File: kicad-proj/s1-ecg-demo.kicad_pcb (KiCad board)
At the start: 4 copper layers, 80.2 x 30.2 mm, 54 parts, among them J1 USB-C-16-Pin, J2 TC2030, J3 Battery Port, J4 Current Probe, J5 ECG_PAD_LA, J6 ECG_PAD_RA, J7 ECG_PAD_RL, U1 AD8233

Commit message: Layout complete, needs checking
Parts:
- removed the R14 at (116.3, 60.6)
- removed the R15 at (114.9, 61.4)
- removed the R16 at (114.9, 59.5)
- removed the R23 at (116.4, 65.0)
- removed the R4 at (118.0, 61.6)
- removed the R6 at (117.7, 64.5)
- removed the TP5 at (113.7, 68.7)
- added FID1: Logo, s1-ecg-demo:sw-logo, B.Cu at (110.9, 103.2)
- added FID2: Board title, s1-ecg-demo:title, B.Cu at (117.2, 103.8)
- added FID3: Heartbeat icon, s1-ecg-demo:heartbeat, F.Cu at (134.8, 106.8)
- added R18: 10M, Resistor_SMD:R_0201_0603Metric, F.Cu at (147.8, 102.7)
- added R19: 10M, Resistor_SMD:R_0201_0603Metric, F.Cu at (146.4, 103.5)
- added R2: 200k, Resistor_SMD:R_0201_0603Metric, F.Cu at (147.8, 101.8)
- added R21: 10M, Resistor_SMD:R_0201_0603Metric, F.Cu at (146.4, 101.6)
- added R22: 5.1k, Resistor_SMD:R_0201_0603Metric, F.Cu at (135.7, 110.3)
- added R3: 499k, Resistor_SMD:R_0201_0603Metric, F.Cu at (150.4, 108.2)
- added TP2: D1, TestPoint:TestPoint_Pad_D1.0mm, B.Cu at (127.4, 106.5)
- J1: renamed from J5; value ECG_PAD_LA -> Left arm
- J2: renamed from J6; value ECG_PAD_RA -> Right arm
- J3: renamed from J7; value ECG_PAD_RL -> Right leg
- JP1: moved to B.Cu
- R1: value 5.1k -> 100k
- R10: value 499k -> 1M
- R11: value 1M -> 182k
- R13: value 182k -> 100k
- R5: value 200k -> 10M
- R7: value 10M -> 100k
- R8: value 100k -> 1M
- R9: value 1M -> 10M
- TP1: value Tp -> ECG out; footprint TestPoint:TestPoint_Pad_1.0x1.0mm -> TestPoint:TestPoint_Pad_D1.0mm; moved to B.Cu
- TP3: renamed from TP2; value Tp -> D2; footprint TestPoint:TestPoint_Pad_1.0x1.0mm -> TestPoint:TestPoint_Pad_D1.0mm; moved to B.Cu
- TP4: renamed from TP3; value Tp -> D3; footprint TestPoint:TestPoint_Pad_1.0x1.0mm -> TestPoint:TestPoint_Pad_D1.0mm; moved to B.Cu
- TP5: renamed from TP4; value Tp -> D4; footprint TestPoint:TestPoint_Pad_1.0x1.0mm -> TestPoint:TestPoint_Pad_D1.0mm; moved to B.Cu
- moved FID4 93.5 mm to (158.2, 117.9)
- moved TP1 75.1 mm to (152.1, 112.8), turned to 0 degrees
- moved TP5 63.1 mm to (127.4, 112.8), turned to 90 degrees
- moved TP4 58.4 mm to (127.4, 110.7), turned to 90 degrees
- moved TP3 58.4 mm to (127.4, 108.6), turned to 90 degrees
- moved R5 57.3 mm to (149.2, 106.6)
- moved FID5 54.9 mm to (120.1, 89.3)
- moved R9 54.4 mm to (150.4, 105.3), turned to 270 degrees
- moved R12 53.3 mm to (149.2, 105.7)
- moved R13 53.0 mm to (147.9, 107.1), turned to 90 degrees
- moved R1 52.7 mm to (149.6, 103.7), turned to 180 degrees
- moved C5 52.6 mm to (147.8, 103.7)
- moved C7 52.6 mm to (145.4, 101.4)
- moved C2 52.6 mm to (145.6, 107.6)
- moved C3 52.6 mm to (149.4, 108.0)
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- renumbered FID3 to FID4, FID4 to FID5, J1 to J4, J2 to J5, J4 to J6, J3 to J7, D1 to LED1, D2 to LED2, D3 to LED3, D4 to LED4, D5 to LED5, D6 to LED6, D7 to LED7, R18 to R14, R19 to R15, R20 to R16, R21 to R17, R22 to R20, R2 to R23, R3 to R4, R17 to R6
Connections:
- net /SWDCLK renamed Net-(J5-Pad4)
- net /SWDIO renamed Net-(J5-Pad2)
- J1 pad 1: Net-(J5-Pad1) -> Net-(J1-Pad1)
- J2 pad 1: Net-(J6-Pad1) -> Net-(J2-Pad1)
- J3 pad 1: Net-(J7-Pad1) -> Net-(J3-Pad1)
- J4 pad A5: Net-(J1-PadA5) -> Net-(J4-PadA5)
- R1 pad 1: GND -> Net-(C1-Pad1)
- R1 pad 2: Net-(J1-PadA5) -> Net-(C4-Pad1)
- R10 pad 1: Net-(C3-Pad1) -> Net-(C4-Pad2)
- R10 pad 2: Net-(J7-Pad1) -> Net-(C2-Pad2)
- R11 pad 1: Net-(C4-Pad2) -> Net-(R11-Pad1)
- R11 pad 2: Net-(C2-Pad2) -> Net-(J1-Pad1)
- R12 pad 2: Net-(J5-Pad1) -> Net-(J2-Pad1)
- R13 pad 1: Net-(R13-Pad1) -> Net-(C4-Pad1)
- R13 pad 2: Net-(J6-Pad1) -> Net-(R13-Pad2)
- R5 pad 1: Net-(C1-Pad1) -> Net-(J2-Pad1)
- R5 pad 2: Net-(C2-Pad2) -> Net-(C3-Pad1)
- R7 pad 1: Net-(J5-Pad1) -> Net-(C4-Pad1)
- R7 pad 2: Net-(C3-Pad1) -> Net-(R7-Pad2)
- R8 pad 1: Net-(C4-Pad1) -> Net-(R7-Pad2)
- R8 pad 2: Net-(R8-Pad2) -> /ECG_OUT
- R9 pad 1: Net-(R8-Pad2) -> Net-(J1-Pad1)
- R9 pad 2: /ECG_OUT -> Net-(C3-Pad1)
- TP1 pad 1: /LED1 -> /ECG_OUT
- U1 pad B5: Net-(R12-Pad1) -> Net-(R11-Pad1)
- U1 pad C5: Net-(R13-Pad1) -> Net-(R12-Pad1)
- U1 pad D2: Net-(R8-Pad2) -> Net-(R7-Pad2)
- U1 pad D4: Net-(R23-Pad2) -> Net-(R13-Pad2)
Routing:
- net Net-(J5-Pad1): track 38.1 -> 0.00 mm, vias 2 -> 0
- net Net-(J1-Pad1): track 0.00 -> 35.5 mm, vias 0 -> 2
- net /LED3: track 5.31 -> 23.5 mm
- net /VBUS: track 6.55 -> 23.9 mm, vias 0 -> 2
- net /VBAT: track 3.65 -> 20.3 mm
- net /ECG_OUT: track 9.51 -> 25.5 mm, vias 0 -> 1
- net /LED4: track 9.86 -> 25.2 mm
- net /LED2: track 6.99 -> 21.8 mm
- net Net-(J2-Pad1): track 0.00 -> 11.6 mm
- net Net-(J3-Pad1): track 0.00 -> 9.50 mm, vias 0 -> 1
- net /LED1: track 8.34 -> 17.0 mm
- net /LOD: track 3.56 -> 11.2 mm
- net Net-(J5-Pad4): track 5.06 -> 9.09 mm
- net Net-(J1-PadA5): track 3.68 -> 0.00 mm, vias 2 -> 0
- net Net-(J5-Pad2): track 7.15 -> 10.7 mm
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- added copper zone on In1.Cu, net +1V8
- added copper zone on B.Cu, net GND
- added copper zone on F.Cu, net GND
- added copper zone on In2.Cu, net GND
- added copper zone on F.Cu, net Net-(J1-Pad1)
- added copper zone on F.Cu, net Net-(J2-Pad1)
- added copper zone on B.Cu, net Net-(J3-Pad1)
- removed copper zone on F.Cu, net Net-(J5-Pad1)
- removed copper zone on F.Cu, net Net-(J6-Pad1)
- removed copper zone on B.Cu, net Net-(J7-Pad1)
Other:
- board text added: "Charging"
- board text added: "D1"
- board text added: "D2"
- board text added: "D3"
- board text added: "D4"
- board text added: "ECG frontend"
- board text added: "ECG out"
- board text added: "I"
- board text added: "Left arm"
- board text added: "Programmer"
- board text added: "Pulse"
- board text added: "Right arm"
- board text added: "Right leg"
- board text added: "S1"
- board text added: "batt"

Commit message: Final check done
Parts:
- added C8: 10u, Capacitor_SMD:C_0402_1005Metric, F.Cu at (144.3, 103.3)
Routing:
- net /ECG_OUT: track 25.5 -> 27.0 mm
- net +1V8: track 6.14 -> 7.24 mm, vias 3 -> 4
- net /LOD: track 11.2 -> 12.3 mm
- net GND: track 2.13 -> 1.80 mm, vias 32 -> 34

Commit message: Little bit of clean up fixed battery and current header re-exported gerbers
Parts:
- moved J6 18.8 mm to (122.5, 96.5), turned to 0 degrees
- moved J7 18.4 mm to (140.3, 102.4), turned to 180 degrees
- moved J5 2.50 mm to (150.8, 94.5), turned to 0 degrees
- moved FID3 0.98 mm to (135.8, 107.0)
- moved JP1 0.45 mm to (123.7, 100.3), turned to 180 degrees
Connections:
- J7 pad 1: Net-(J6-Pad2) -> GND
- J7 pad 2: GND -> Net-(J6-Pad2)
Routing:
- net /VBUS: track 23.9 -> 7.98 mm, vias 2 -> 5
- net /VBAT: track 20.3 -> 31.0 mm, vias 1 -> 2
- net +1V8: track 7.24 -> 12.0 mm, vias 4 -> 12
- net Net-(J3-Pad1): track 9.50 -> 12.6 mm
- net Net-(C4-Pad1): track 7.23 -> 10.1 mm
- net Net-(J5-Pad2): track 10.7 -> 8.07 mm
- net Net-(J2-Pad1): track 11.6 -> 14.0 mm
- net Net-(J6-Pad2): track 19.8 -> 18.4 mm
- net /~SDN: track 17.6 -> 16.4 mm
- net GND: track 1.80 -> 3.00 mm, vias 34 -> 66
- net /ECG_OUT: track 27.0 -> 26.2 mm
- net /LED2: track 21.8 -> 22.3 mm
- added copper zone on In1.Cu, net /VBUS
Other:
- board text added: "Battery"
- board text added: "Center"
- board text added: "Cut for current measurement"
- board text added: "Debug"
- board text added: "S1 module"
- board text removed: "Programmer"
- board text removed: "S1"

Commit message: Final files ready for order
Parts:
- removed the R13 at (147.9, 107.1)
- C1: renamed from C5; value 0.22u -> 220nF
- C2: renamed from C1; value 0.22u -> 220nF
- C3: renamed from C7; value 1u -> 1uF
- C4: renamed from C3; value 1n -> 1nF
- C5: renamed from C6; value 0.1u -> 100nF
- C6: renamed from C8; value 10u -> 10uF
- C7: renamed from C4; value 22n -> 22nF
- C8: renamed from C2; value 10n -> 10nF
- R16: renamed from R4; value 665 -> 665R
- R17: renamed from R6; value 665 -> 665R
- R18: renamed from R14; value 665 -> 665R
- R19: renamed from R15; value 665 -> 665R
- R20: renamed from R16; value 665 -> 665R
- R21: renamed from R17; value 665 -> 665R
- R22: renamed from R20; value 665 -> 665R
- U1: footprint s1-ecg-demo:WLCSP-20 -> s1-ecg-demo:WLCSP-20-no-paste
- moved R11 3.74 mm to (148.0, 107.1), turned to 90 degrees
- renumbered J5 to J2, J2 to J3, J3 to J4, J6 to J5, J4 to J6, R18 to R1, R1 to R11, R7 to R12, R8 to R13, R22 to R14, R23 to R15, R11 to R2, R12 to R3, R19 to R4, R9 to R6, R21 to R7, R3 to R8, R2 to R9
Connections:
- net /ECG_OUT renamed /ecg-out
- net /LED1 renamed /led1
- net /LED2 renamed /led2
- net /LED3 renamed /led3
- net /LED4 renamed /led4
- net /LED5 renamed /led5
- net /LED6 renamed /led6
- net /LED7 renamed /led7
- net /LOD renamed /lead-detect
- net /VBAT renamed /Vbatt
- net /VBUS renamed VBUS
- net /~SDN renamed /~shutdown
- C1 pad 2: Net-(C5-Pad2) -> Net-(C1-Pad2)
- C2 pad 1: Net-(C1-Pad1) (its old number) -> Net-(C2-Pad1)
- C2 pad 2: Net-(C1-Pad2) -> Net-(C2-Pad2)
- C7 pad 1: Net-(C4-Pad1) (its old number) -> Net-(C7-Pad1)
- J6 pad A6: (no net) -> Net-(J6-PadA6)
- J6 pad A7: (no net) -> Net-(J6-PadA7)
- J6 pad B6: (no net) -> Net-(J6-PadA6)
- J6 pad B7: (no net) -> Net-(J6-PadA7)
- R1 pad 1: Net-(C5-Pad2) -> Net-(C2-Pad2)
- R11 pad 1: Net-(C1-Pad1) (its old number) -> Net-(C7-Pad1)
- R11 pad 2: Net-(C4-Pad1) (its old number) -> Net-(C2-Pad1)
- R12 pad 1: Net-(C4-Pad1) (its old number) -> Net-(C7-Pad1)
- R9 pad 1: Net-(C1-Pad1) (its old number) -> Net-(C2-Pad1)
- U1 pad A4: Net-(C5-Pad2) -> Net-(C1-Pad2)
- U1 pad B4: Net-(C1-Pad2) -> Net-(C2-Pad2)
- U1 pad C3: Net-(C4-Pad1) (its old number) -> Net-(C7-Pad1)
- U1 pad D4: Net-(R13-Pad2) -> Net-(C2-Pad1)
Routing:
- net Net-(C4-Pad1) (its old number): track 10.1 -> 0.00 mm, vias 4 -> 0
- net Net-(C2-Pad1): track 0.00 -> 6.88 mm, vias 0 -> 2
- net Net-(C2-Pad2): track 0.00 -> 4.74 mm, vias 0 -> 2
- net Net-(C7-Pad1): track 0.00 -> 4.38 mm, vias 0 -> 3
- net Net-(C1-Pad1) (its old number): track 3.19 -> 0.00 mm
- net Net-(C5-Pad2): track 2.21 -> 0.00 mm
- net Net-(C1-Pad2): track 3.69 -> 2.44 mm, vias 2 -> 0
- net Net-(R13-Pad2): track 1.02 -> 0.00 mm
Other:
- board text added: "+"

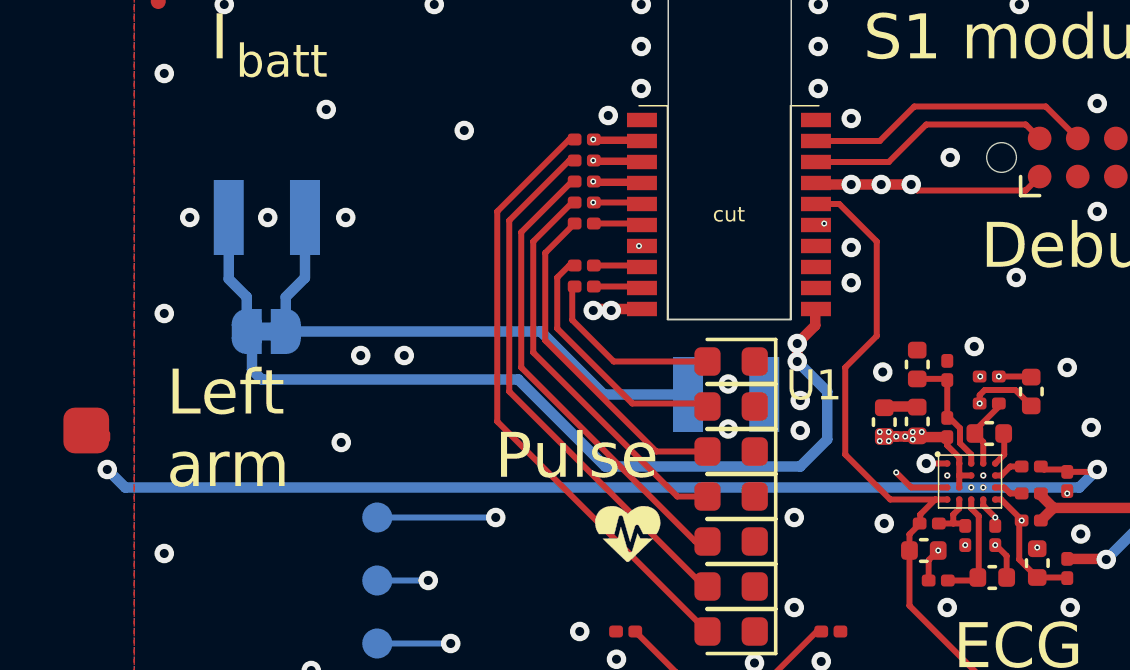
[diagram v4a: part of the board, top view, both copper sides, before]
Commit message: Added shutdown pullup resistor Adjusted current probe header location Updated BOM Exported v2 gerber
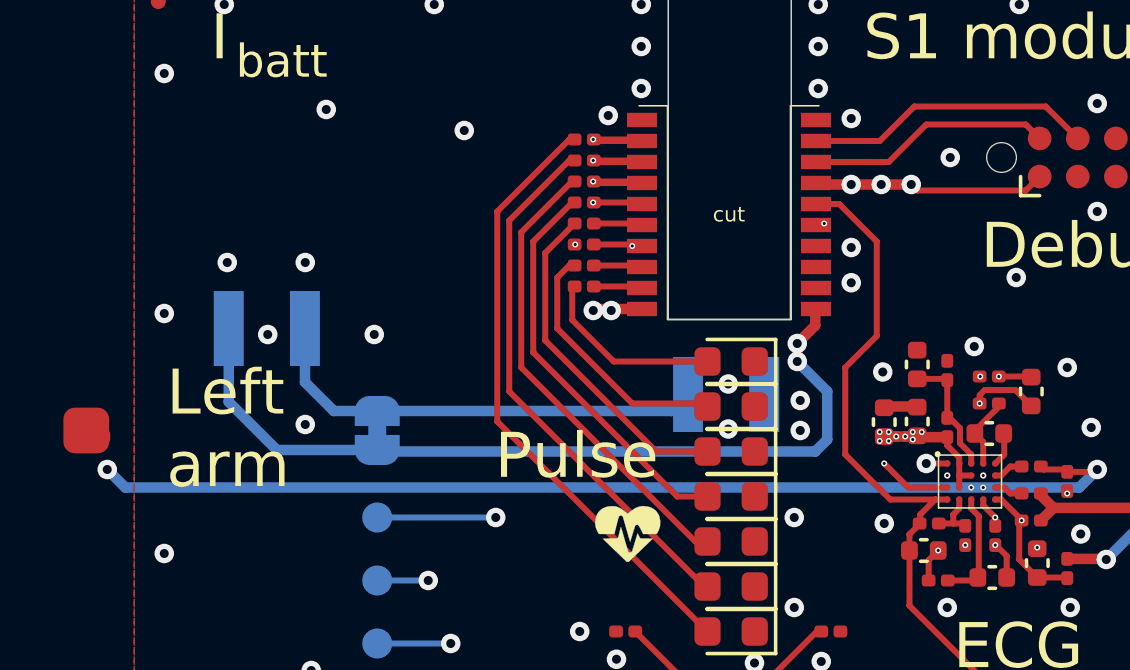
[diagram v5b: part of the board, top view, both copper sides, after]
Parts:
- added R3: 10M, Resistor_SMD:R_0201_0603Metric, F.Cu at (134.3, 97.4)
- moved JP1 4.96 mm to (127.4, 103.6), turned to 270 degrees
- moved J5 3.70 mm to (122.5, 100.2)
- renumbered R9 to R10, R10 to R11, R11 to R12, R12 to R13, R13 to R14, R14 to R15, R15 to R16, R16 to R17, R17 to R18, R18 to R19, R19 to R20, R20 to R21, R21 to R22, R22 to R23, R3 to R4, R4 to R5, R5 to R6, R6 to R7, R7 to R8, R8 to R9
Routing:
- net +1V8: track 12.0 -> 29.8 mm, vias 12 -> 13
- net Net-(J5-Pad2): track 18.4 -> 15.2 mm
- net /Vbatt: track 31.0 -> 28.2 mm
- net /~shutdown: track 16.4 -> 18.2 mm
- net GND: vias 66 -> 65

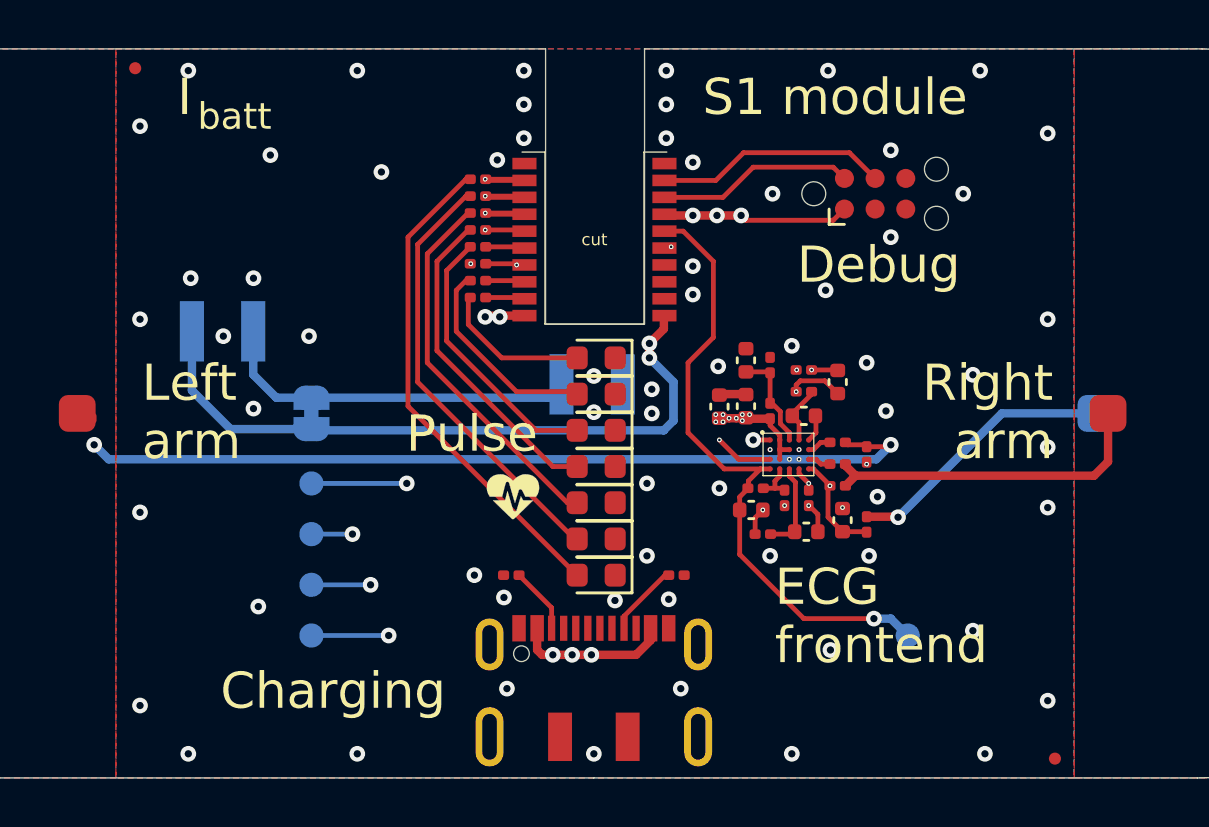
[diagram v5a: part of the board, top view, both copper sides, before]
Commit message: Fixed ground break Isolation around battery positive terminal Removed the cuttable jumper Cleaned up silkscreen Added 0.1" pin jumper to BOM
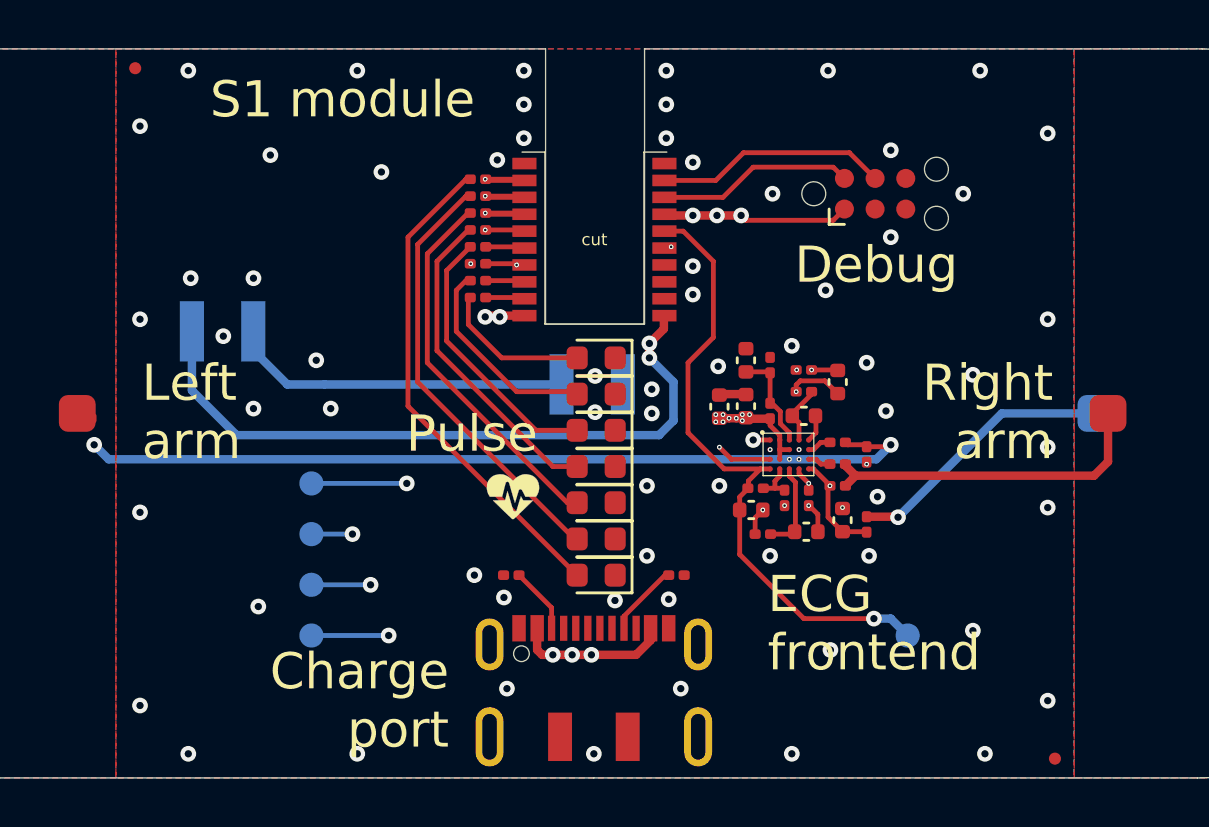
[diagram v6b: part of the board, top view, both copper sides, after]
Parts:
- removed JP1: Jumper_NC_Small, Jumper:SolderJumper-2_P1.3mm_Bridged_RoundedPad1.0x1.5mm
- J5: value Current Probe -> Current Measure
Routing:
- net Net-(J5-Pad2): track 15.2 -> 14.1 mm
- net /lead-detect: track 12.1 -> 11.4 mm
- net GND: vias 65 -> 66
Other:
- board text added: "Battery current"
- board text added: "Charge port"
- board text removed: "Charging"
- board text removed: "Cut for current measurement"
- board text removed: "I"
- board text removed: "batt"

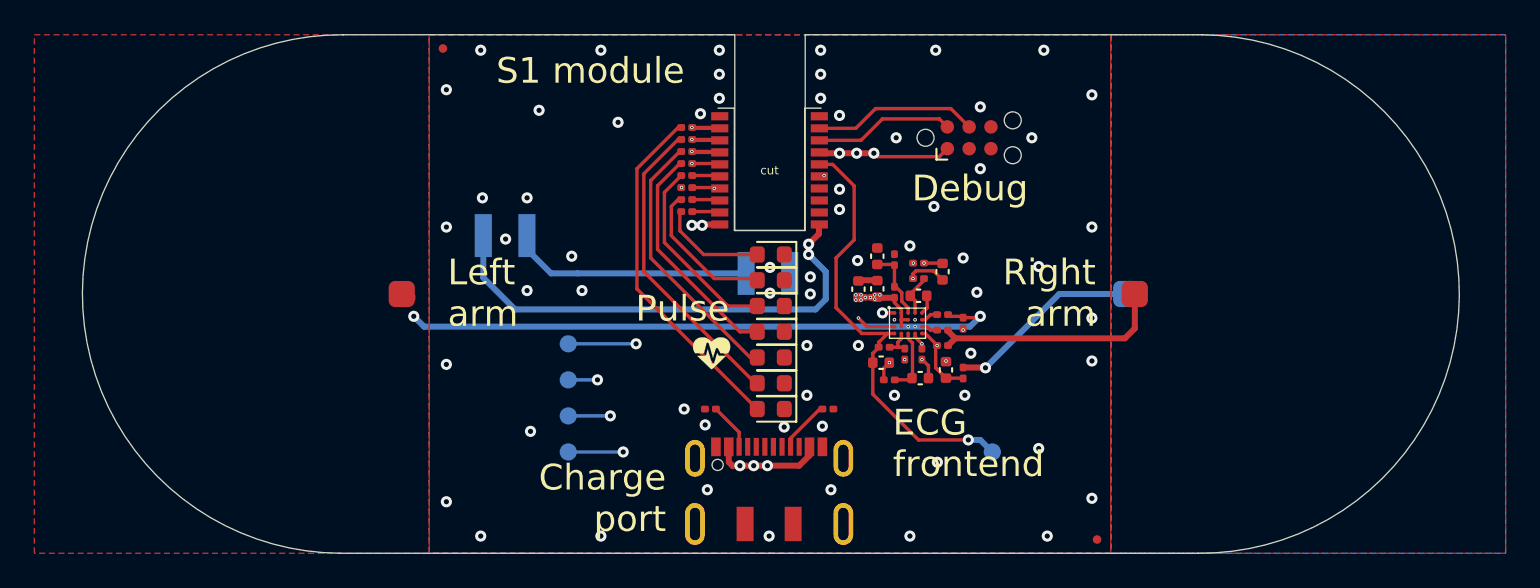
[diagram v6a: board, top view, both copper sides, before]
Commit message: Migrated to Kicad 6 Re-exported gerbers with correct WLCSP paste layer
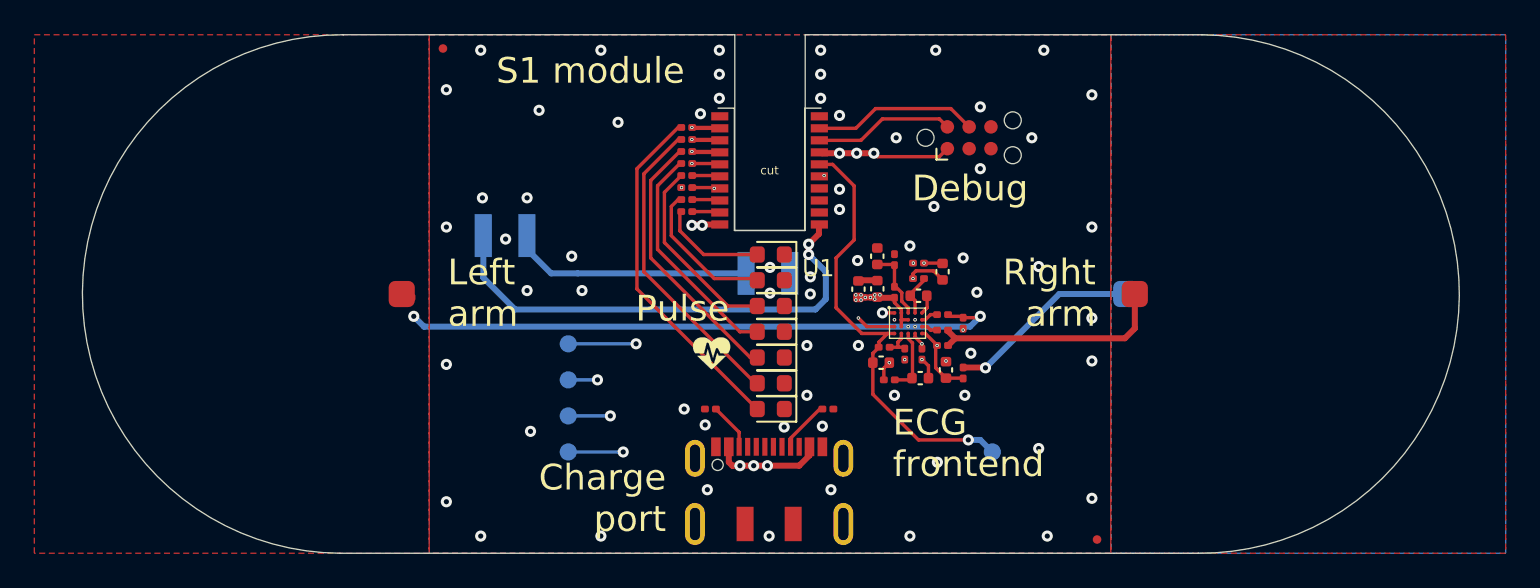
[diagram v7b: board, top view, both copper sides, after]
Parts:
- U1: footprint s1-ecg-demo:WLCSP-20-no-paste -> s1-ecg-demo:WLCSP-20
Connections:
- net /~shutdown renamed /~{shutdown}
- J2 pad 3: (no net) -> unconnected-(J2-Pad3)
- J2 pad 6: (no net) -> unconnected-(J2-Pad6)
- J6 pad A6: Net-(J6-PadA6) -> unconnected-(J6-PadA6)
- J6 pad A7: Net-(J6-PadA7) -> unconnected-(J6-PadA7)
- J6 pad B6: Net-(J6-PadA6) -> unconnected-(J6-PadA6)
- J6 pad B7: Net-(J6-PadA7) -> unconnected-(J6-PadA7)
- MOD1 pad 12: (no net) -> unconnected-(MOD1-Pad12)
- MOD1 pad 13: (no net) -> unconnected-(MOD1-Pad13)
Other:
- net class Default removed
